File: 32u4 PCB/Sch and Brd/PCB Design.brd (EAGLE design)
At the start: 71.6 x 74.8 mm, 62 parts, among them Q1 16MHz

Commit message: Changed values and modified BOM
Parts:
- R11, R18, R7, R9: value 330 -> 1k
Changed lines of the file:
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@@
 <attribute name="VALUE" x="40.64" y="18.288" size="0.6096" layer="27" font="vector" ratio="20" rot="R180" align="top-center"/>
 </element>
-<element name="R9" library="resistor" library_urn="urn:adsk.eagle:library:348" package="M0805" value="330" x="36.068" y="18.034" smashed="yes">
+<element name="R9" library="resistor" library_urn="urn:adsk.eagle:library:348" package="M0805" value="1k" x="36.068" y="18.034" smashed="yes">
 <attribute name="MF" value="" x="36.068" y="18.034" size="1.778" layer="27" display="off"/>
 <attribute name="MPN" value="" x="36.068" y="18.034" size="1.778" layer="27" display="off"/>
@@
 <attribute name="VALUE" x="63.119" y="-0.254" size="0.6096" layer="27" font="vector" ratio="20" rot="R270" align="top-center"/>
 </element>
-<element name="R18" library="resistor" library_urn="urn:adsk.eagle:library:348" package="M0805" value="330" x="69.342" y="-2.794" smashed="yes" rot="R180">
+<element name="R18" library="resistor" library_urn="urn:adsk.eagle:library:348" package="M0805" value="1k" x="69.342" y="-2.794" smashed="yes" rot="R180">
 <attribute name="MF" value="" x="69.342" y="-2.794" size="1.778" layer="27" rot="R180" display="off"/>
 <attribute name="MPN" value="" x="69.342" y="-2.794" size="1.778" layer="27" rot="R180" display="off"/>
@@
 <attribute name="VALUE" x="40.64" y="16.383" size="0.6096" layer="27" font="vector" ratio="20" rot="R180" align="top-center"/>
 </element>
-<element name="R11" library="resistor" library_urn="urn:adsk.eagle:library:348" package="M0805" value="330" x="36.068" y="15.748" smashed="yes">
+<element name="R11" library="resistor" library_urn="urn:adsk.eagle:library:348" package="M0805" value="1k" x="36.068" y="15.748" smashed="yes">
 <attribute name="MF" value="" x="36.068" y="12.7" size="1.778" layer="27" display="off"/>
 <attribute name="MPN" value="" x="36.068" y="12.7" size="1.778" layer="27" display="off"/>
@@
 <attribute name="VALUE" x="40.64" y="20.193" size="0.6096" layer="27" font="vector" ratio="20" rot="R180" align="top-center"/>
 </element>
-<element name="R7" library="resistor" library_urn="urn:adsk.eagle:library:348" package="M0805" value="330" x="31.75" y="20.32" smashed="yes">
+<element name="R7" library="resistor" library_urn="urn:adsk.eagle:library:348" package="M0805" value="1k" x="31.75" y="20.32" smashed="yes">
 <attribute name="MF" value="" x="31.75" y="17.272" size="1.778" layer="27" display="off"/>
 <attribute name="MPN" value="" x="31.75" y="17.272" size="1.778" layer="27" display="off"/>

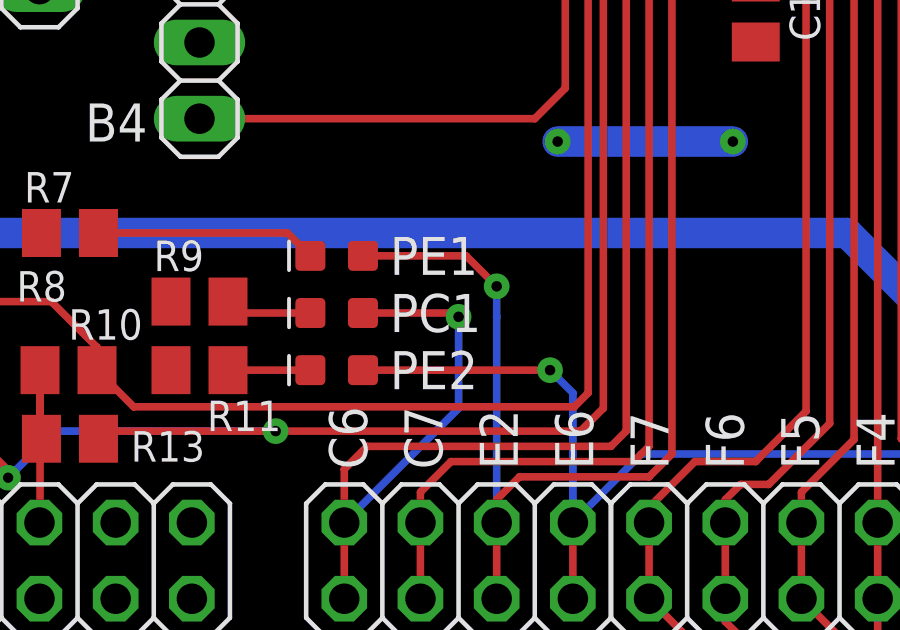
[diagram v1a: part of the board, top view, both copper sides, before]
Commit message: Changed Silkscreen
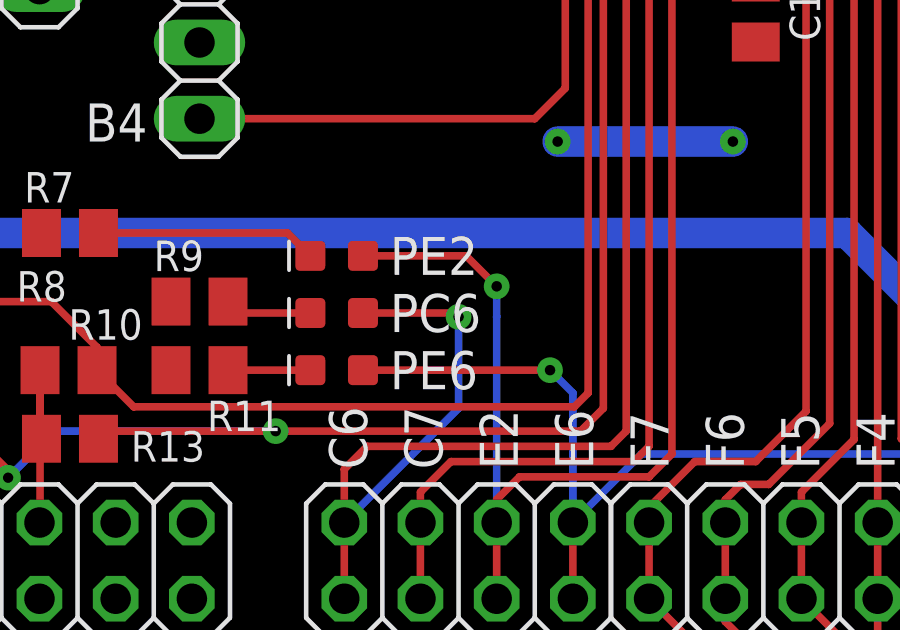
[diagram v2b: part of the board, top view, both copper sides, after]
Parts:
- removed PE1: Yellow, SparkFun-LED:LED-0603
- added PE6: Blue, SparkFun-LED:LED-0603
- PC6, PE2: value Yellow -> Blue
- moved PE2 3.81 mm to (40.6, 19.6)
- renumbered PC1 to PC6
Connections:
- net N$3: now also PE6.C; no longer PE2.C
- net N$7: now also PE2.C; no longer PE1.C
- net PE2: now also PE2.A; no longer PE1.A
- net PE6: now also PE6.A; no longer PE2.A
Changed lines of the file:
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@@
 <attribute name="VALUE" x="24.765" y="15.875" size="1.27" layer="27" ratio="10"/>
 </element>
-<element name="PC1" library="SparkFun-LED" package="LED-0603" value="Yellow" x="40.64" y="17.653" smashed="yes" rot="R180">
+<element name="PC6" library="SparkFun-LED" package="LED-0603" value="Blue" x="40.64" y="17.653" smashed="yes" rot="R180">
 <attribute name="MF" value="" x="40.64" y="17.653" size="1.778" layer="27" rot="R180" display="off"/>
 <attribute name="MPN" value="" x="40.64" y="17.653" size="1.778" layer="27" rot="R180" display="off"/>
@@
 <attribute name="VALUE" x="62.484" y="53.975" size="0.6096" layer="27" font="vector" ratio="20"/>
 </element>
-<element name="PE2" library="SparkFun-LED" package="LED-0603" value="Yellow" x="40.64" y="15.748" smashed="yes" rot="R180">
+<element name="PE6" library="SparkFun-LED" package="LED-0603" value="Blue" x="40.64" y="15.748" smashed="yes" rot="R180">
 <attribute name="MF" value="" x="40.386" y="9.398" size="1.778" layer="27" rot="R180" display="off"/>
 <attribute name="MPN" value="" x="40.386" y="9.398" size="1.778" layer="27" rot="R180" display="off"/>
@@
 <attribute name="VALUE" x="34.798" y="13.208" size="1.27" layer="27"/>
 </element>
-<element name="PE1" library="SparkFun-LED" package="LED-0603" value="Yellow" x="40.64" y="19.558" smashed="yes" rot="R180">
+<element name="PE2" library="SparkFun-LED" package="LED-0603" value="Blue" x="40.64" y="19.558" smashed="yes" rot="R180">
 <attribute name="MF" value="" x="40.386" y="13.208" size="1.778" layer="27" rot="R180" display="off"/>
 <attribute name="MPN" value="" x="40.386" y="13.208" size="1.778" layer="27" rot="R180" display="off"/>
@@
 </signal>
 <signal name="N$1">
-<contactref element="PC1" pad="C"/>
+<contactref element="PC6" pad="C"/>
 <contactref element="R9" pad="2"/>
 <wire x1="39.763" y1="17.653" x2="37.399" y2="17.653" width="0.254" layer="1"/>
@@
 </signal>
 <signal name="N$3">
-<contactref element="PE2" pad="C"/>
+<contactref element="PE6" pad="C"/>
 <contactref element="R11" pad="2"/>
 <wire x1="39.763" y1="15.748" x2="37.018" y2="15.748" width="0.254" layer="1"/>
 </signal>
 <signal name="N$7">
-<contactref element="PE1" pad="C"/>
+<contactref element="PE2" pad="C"/>
 <contactref element="R7" pad="2"/>
 <wire x1="32.7" y1="20.32" x2="39.001" y2="20.32" width="0.254" layer="1"/>
@@
 <wire x1="45.974" y1="10.668" x2="45.974" y2="8.128" width="0.254" layer="1"/>
 <wire x1="52.9336" y1="32.5882" x2="51.816" y2="31.4706" width="0.254" layer="1"/>
-<contactref element="PE1" pad="A"/>
+<contactref element="PE2" pad="A"/>
 <wire x1="51.816" y1="31.4706" x2="51.816" y2="12.954" width="0.254" layer="1"/>
 <wire x1="45.974" y1="10.668" x2="45.974" y2="11.43" width="0.254" layer="1"/>
@@
 <wire x1="48.514" y1="10.668" x2="50.8" y2="12.954" width="0.254" layer="16"/>
 <wire x1="50.8" y1="12.954" x2="65.024" y2="12.954" width="0.254" layer="16"/>
-<contactref element="PE2" pad="A"/>
+<contactref element="PE6" pad="A"/>
 <wire x1="65.024" y1="31.9786" x2="65.024" y2="12.954" width="0.254" layer="1"/>
 <wire x1="64.4144" y1="32.5882" x2="65.024" y2="31.9786" width="0.254" layer="1"/>
@@
 <wire x1="40.894" y1="10.668" x2="40.894" y2="12.446" width="0.254" layer="1"/>
 <wire x1="40.894" y1="12.446" x2="41.656" y2="13.208" width="0.254" layer="1"/>
-<contactref element="PC1" pad="A"/>
+<contactref element="PC6" pad="A"/>
 <wire x1="40.894" y1="8.128" x2="40.894" y2="10.668" width="0.254" layer="1"/>
 <wire x1="51.562" y1="34.1884" x2="50.292" y2="32.9184" width="0.254" layer="1"/>
